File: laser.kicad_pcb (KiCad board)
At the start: 4 copper layers, 90.2 x 50.9 mm, 128 parts, among them IC201 ADM7172ACPZ-4.2-R7, IC202 LT1716CS5#TRPBF, IC203 ADM7154ARDZ-3.3-R7, IC204 IRF9358PBF, IC601 ATMEGA328P-AU, IC602 FT232RL-TUBE, IC701 MAX6126AASA25+, IC801 ADS122C04IPWR, J601 M20-9980345, J602 USB_Connector, Q401 RSR030N06TL, U101 281698-3, U201 LM4040EIM3X-2.5_NOPB, U301 OPA569AIDWPR, U302 OPA569AIDWPR, U401 ADA4528-2ACPZ-RL, U402 782853152_WE-CBA_08, U501 ADA4528-2ACPZ-RL, U502 ADA4528-2ACPZ-RL, U801 MAX5217GUA+, U802 MAX5217GUA+, Y601 ECS-160-16-33B-CKM-TR

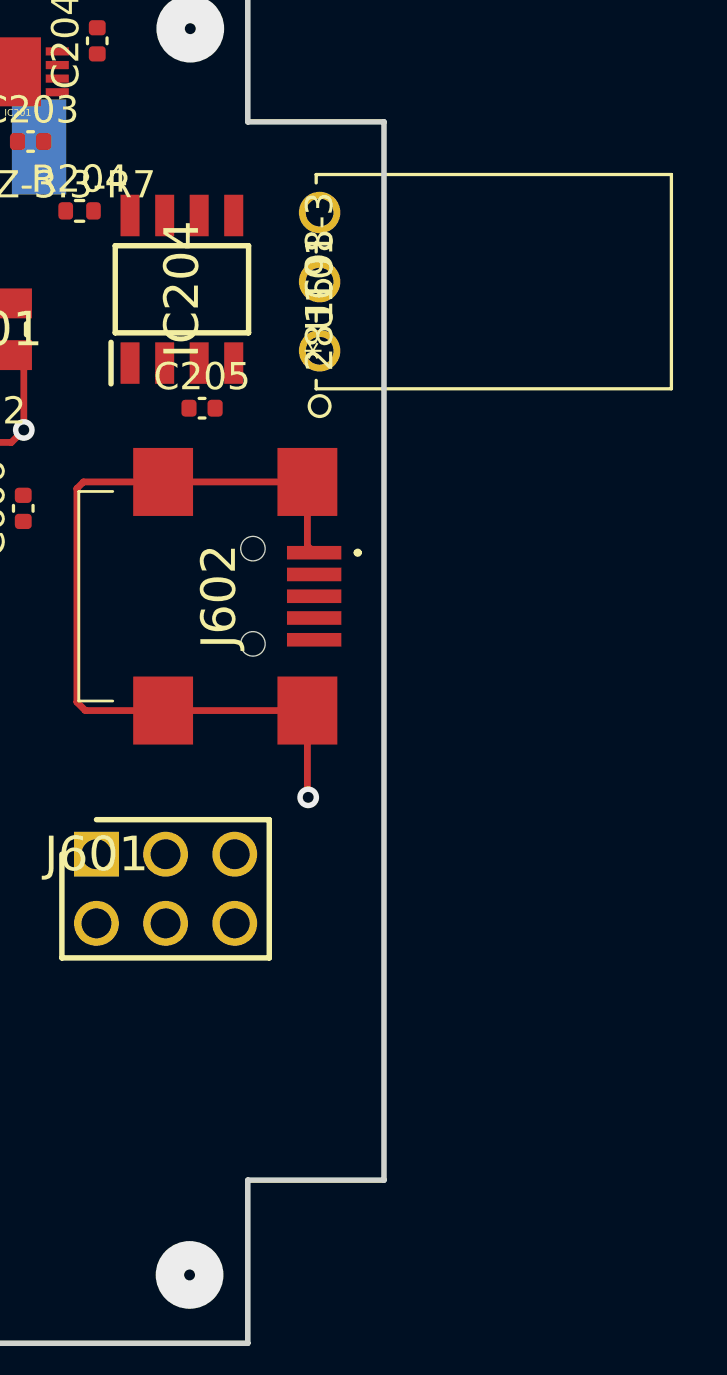
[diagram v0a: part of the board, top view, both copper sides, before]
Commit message: added 5V
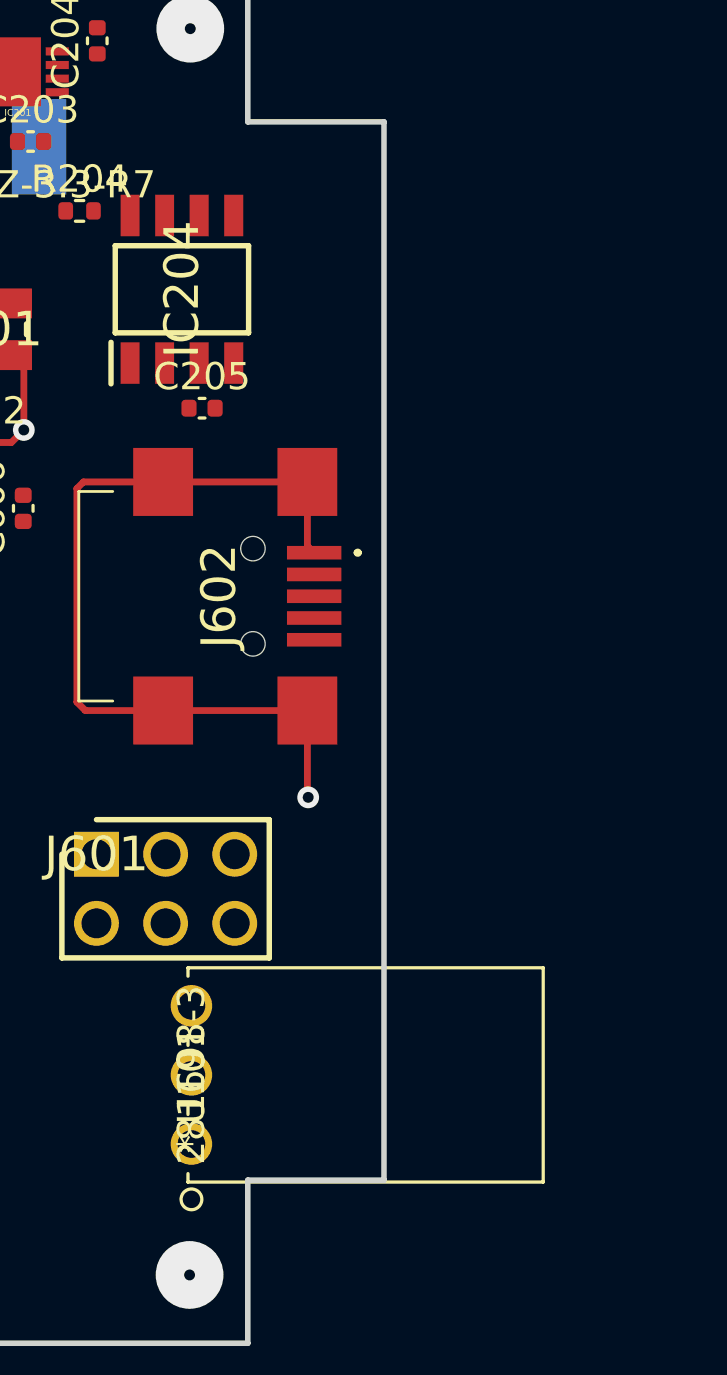
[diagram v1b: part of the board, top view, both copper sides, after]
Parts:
- moved U101 29.5 mm to (205.9, 124.9)
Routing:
- added copper zone on PWR, net 5.0V
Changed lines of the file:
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@@
     (0 F.Cu signal)
     (1 GND power hide)
-    (2 PWR power)
+    (2 PWR power hide)
     (31 B.Cu signal)
     (32 B.Adhes user)
@@
   )
   (module "footprint libraries:281698-3" (layer F.Cu)
-    (at 210.62 95.74 90)
+    (at 205.91 124.89 90)
     (fp_text reference U101 (at 2.54 0 90) (layer F.SilkS)
       (effects (font (size 1 1) (thickness 0.15)))
@@
       (effects (font (size 1 1) (thickness 0.15)))
     )
-    (fp_line (start -1.397 12.927) (end 6.477 12.927) (layer F.SilkS) (width 0.12))
-    (fp_line (start 6.477 12.927) (end 6.477 -0.127) (layer F.SilkS) (width 0.12))
-    (fp_line (start 6.477 -0.127) (end 6.167348 -0.127) (layer F.SilkS) (width 0.12))
-    (fp_line (start -1.397 -0.127) (end -1.397 12.927) (layer F.SilkS) (width 0.12))
-    (fp_line (start -1.27 12.8) (end 6.35 12.8) (layer F.Fab) (width 0.1))
-    (fp_line (start 6.35 12.8) (end 6.35 0) (layer F.Fab) (width 0.1))
-    (fp_line (start 6.35 0) (end -1.27 0) (layer F.Fab) (width 0.1))
-    (fp_line (start -1.27 0) (end -1.27 12.8) (layer F.Fab) (width 0.1))
-    (fp_line (start -1.087348 -0.127) (end -1.397 -0.127) (layer F.SilkS) (width 0.12))
-    (fp_line (start 1.452652 -0.127) (end 1.087348 -0.127) (layer F.SilkS) (width 0.12))
-    (fp_line (start 3.992652 -0.127) (end 3.627348 -0.127) (layer F.SilkS) (width 0.12))
-    (fp_line (start -1.524 -1.016) (end -1.524 13.054) (layer F.CrtYd) (width 0.05))
-    (fp_line (start -1.524 13.054) (end 6.604 13.054) (layer F.CrtYd) (width 0.05))
-    (fp_line (start 6.604 13.054) (end 6.604 -1.016) (layer F.CrtYd) (width 0.05))
-    (fp_line (start 6.604 -1.016) (end -1.524 -1.016) (layer F.CrtYd) (width 0.05))
-    (fp_circle (center -2.032 0) (end -1.651 0) (layer F.SilkS) (width 0.12))
-    (fp_circle (center -2.032 0) (end -1.651 0) (layer B.SilkS) (width 0.12))
-    (fp_circle (center 0 -1.905) (end 0.381 -1.905) (layer F.Fab) (width 0.1))
-    (fp_text user "Copyright 2021 Accelerated Designs. All rights reserved." (at 0 0 90) (layer Cmts.User)
-      (effects (font (size 0.127 0.127) (thickness 0.002)))
+    (fp_text user * (at 0 0 90) (layer F.Fab)
+      (effects (font (size 1 1) (thickness 0.15)))
     )
     (fp_text user * (at 0 0 90) (layer F.SilkS)
       (effects (font (size 1 1) (thickness 0.15)))
     )
-    (fp_text user * (at 0 0 90) (layer F.Fab)
-      (effects (font (size 1 1) (thickness 0.15)))
+    (fp_text user "Copyright 2021 Accelerated Designs. All rights reserved." (at 0 0 90) (layer Cmts.User)
+      (effects (font (size 0.127 0.127) (thickness 0.002)))
     )
-    (pad 1 thru_hole circle (at 0 0 90) (size 1.524 1.524) (drill 1.016) (layers *.Cu *.Mask)
-      (net 119 GND))
-    (pad 2 thru_hole circle (at 2.54 0 90) (size 1.524 1.524) (drill 1.016) (layers *.Cu *.Mask)
-      (net 40 5V_EXTERNAL_Power_Source))
+    (fp_circle (center 0 -1.905) (end 0.381 -1.905) (layer F.Fab) (width 0.1))
+    (fp_circle (center -2.032 0) (end -1.651 0) (layer B.SilkS) (width 0.12))
+    (fp_circle (center -2.032 0) (end -1.651 0) (layer F.SilkS) (width 0.12))
+    (fp_line (start 6.604 -1.016) (end -1.524 -1.016) (layer F.CrtYd) (width 0.05))
+    (fp_line (start 6.604 13.054) (end 6.604 -1.016) (layer F.CrtYd) (width 0.05))
+    (fp_line (start -1.524 13.054) (end 6.604 13.054) (layer F.CrtYd) (width 0.05))
+    (fp_line (start -1.524 -1.016) (end -1.524 13.054) (layer F.CrtYd) (width 0.05))
+    (fp_line (start 3.992652 -0.127) (end 3.627348 -0.127) (layer F.SilkS) (width 0.12))
+    (fp_line (start 1.452652 -0.127) (end 1.087348 -0.127) (layer F.SilkS) (width 0.12))
+    (fp_line (start -1.087348 -0.127) (end -1.397 -0.127) (layer F.SilkS) (width 0.12))
+    (fp_line (start -1.27 0) (end -1.27 12.8) (layer F.Fab) (width 0.1))
+    (fp_line (start 6.35 0) (end -1.27 0) (layer F.Fab) (width 0.1))
+    (fp_line (start 6.35 12.8) (end 6.35 0) (layer F.Fab) (width 0.1))
+    (fp_line (start -1.27 12.8) (end 6.35 12.8) (layer F.Fab) (width 0.1))
+    (fp_line (start -1.397 -0.127) (end -1.397 12.927) (layer F.SilkS) (width 0.12))
+    (fp_line (start 6.477 -0.127) (end 6.167348 -0.127) (layer F.SilkS) (width 0.12))
+    (fp_line (start 6.477 12.927) (end 6.477 -0.127) (layer F.SilkS) (width 0.12))
+    (fp_line (start -1.397 12.927) (end 6.477 12.927) (layer F.SilkS) (width 0.12))
     (pad 3 thru_hole circle (at 5.08 0 90) (size 1.524 1.524) (drill 1.016) (layers *.Cu *.Mask)
       (net 21 MODULATION_SIGNAL))
+    (pad 2 thru_hole circle (at 2.54 0 90) (size 1.524 1.524) (drill 1.016) (layers *.Cu *.Mask)
+      (net 40 5V_EXTERNAL_Power_Source))
+    (pad 1 thru_hole circle (at 0 0 90) (size 1.524 1.524) (drill 1.016) (layers *.Cu *.Mask)
+      (net 119 GND))
   )
   (module "footprint libraries:LM4040EIM3X-2.5&slash_NOPB" (layer F.Cu)
@@
       )
     )
+  )
+  (zone (net 16) (net_name 5.0V) (layer PWR) (hatch edge 0.508)
+    (connect_pads (clearance 0.508))
+    (min_thickness 0.254)
+    (fill yes (arc_segments 32) (thermal_gap 0.508) (thermal_bridge_width 0.508))
+    (polygon
+      (pts
+        (xy 208.01 132.65) (xy 201.04 132.65) (xy 201.04 119.66) (xy 187.17 119.66) (xy 187.17 81.02)
+        (xy 208.01 80.95)
+      )
+    )

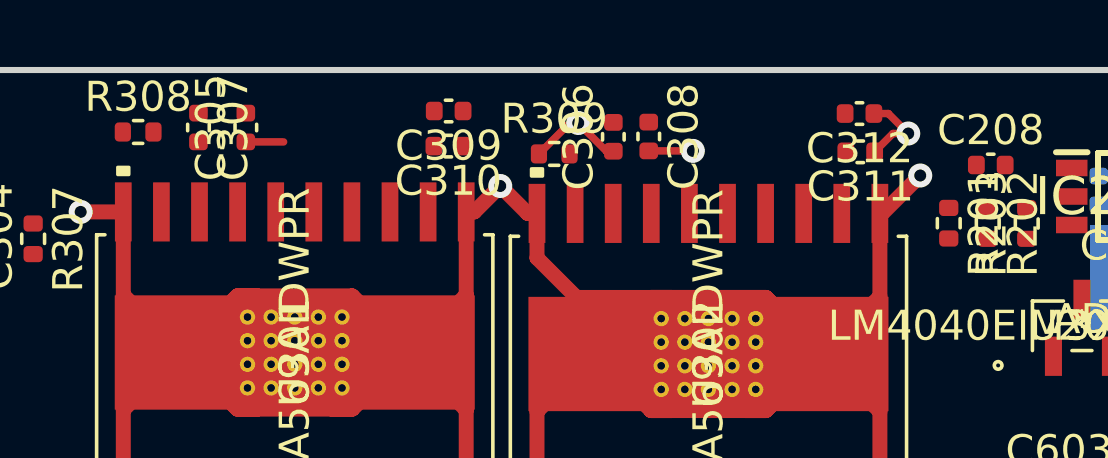
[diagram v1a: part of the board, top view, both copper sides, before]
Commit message: update power op amps sch
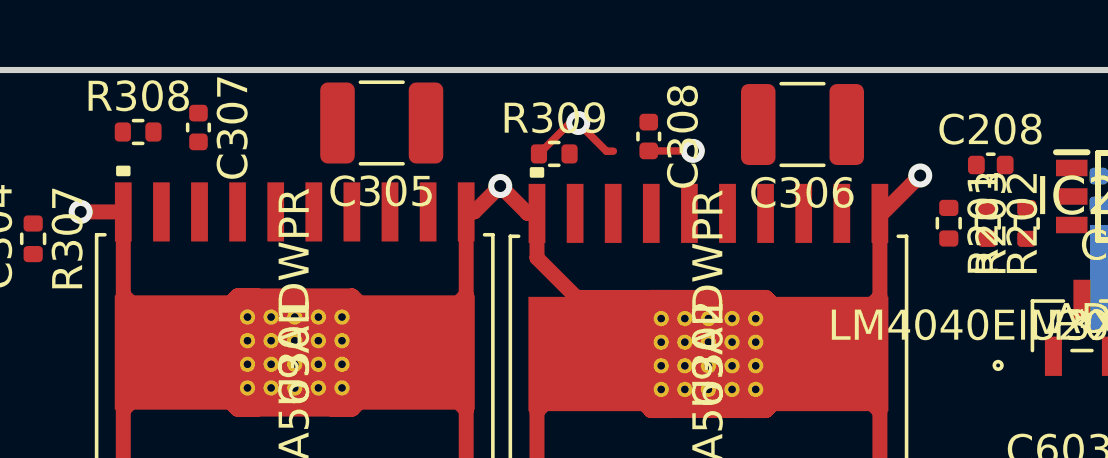
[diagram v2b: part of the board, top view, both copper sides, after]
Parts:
- removed C309, C311: 1u, Capacitor_SMD:C_0402_1005Metric
- removed C310, C312: 0.1u, Capacitor_SMD:C_0402_1005Metric
- C305, C306: footprint Capacitor_SMD:C_0402_1005Metric -> Capacitor_SMD:C_1210_3225Metric
- moved C306 6.32 mm to (180.7, 83.2), turned to 180 degrees
- moved C305 4.53 mm to (166.7, 83.1), turned to 180 degrees
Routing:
- net GND: track 208.4 -> 204.3 mm, vias 38 -> 37

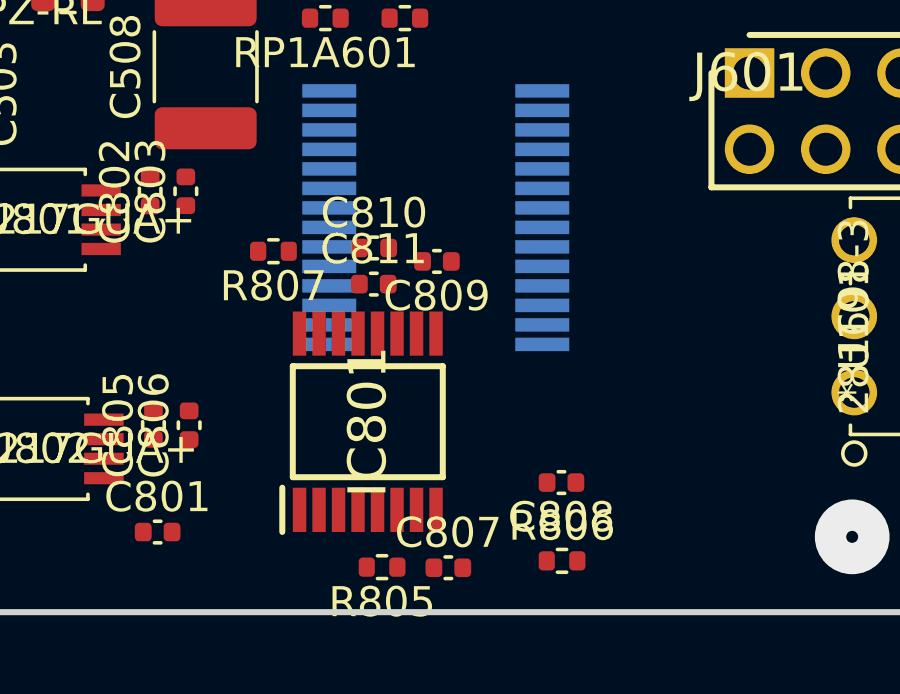
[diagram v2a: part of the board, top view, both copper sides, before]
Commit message: added 3.3
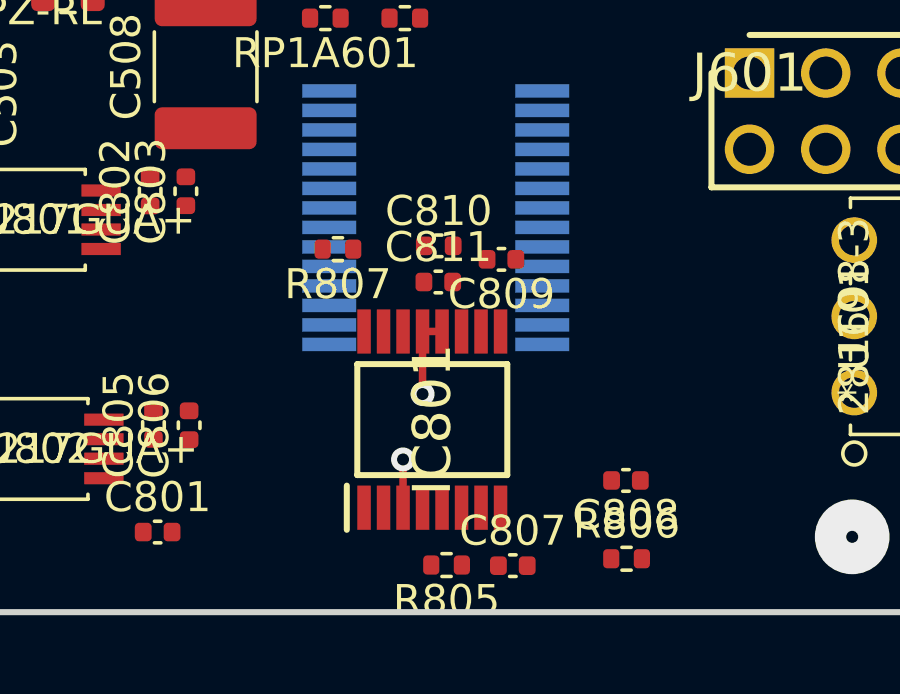
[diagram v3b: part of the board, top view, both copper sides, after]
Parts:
- moved R805 2.15 mm to (192.3, 130.6)
- moved C808 2.15 mm to (198.3, 127.8)
- moved C811 2.15 mm to (192.0, 121.2)
- moved C807 2.15 mm to (194.5, 130.7)
- moved C809 2.15 mm to (194.2, 120.5)
- moved C810 2.15 mm to (192.1, 120.0)
- moved IC801 2.15 mm to (191.8, 125.8)
- moved R806 2.15 mm to (198.3, 130.4)
- moved R807 2.15 mm to (188.7, 120.1)
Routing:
- net 3.3V: track 0.00 -> 4.35 mm, vias 0 -> 2
- added copper zone on PWR, net 3.3V

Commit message: added half a trace for 5v ext
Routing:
- net 5V_EXTERNAL_Power_Source: track 0.00 -> 31.5 mm
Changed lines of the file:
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@@
     (thickness 1.6)
     (drawings 17)
-    (tracks 191)
+    (tracks 194)
     (zones 0)
     (modules 124)
@@
   )
   (setup
-    (last_trace_width 2)
+    (last_trace_width 1.8)
     (user_trace_width 0.5)
-    (user_trace_width 2)
+    (user_trace_width 1.8)
     (trace_clearance 0.2)
     (zone_clearance 0.508)
@@
   (segment (start 190.87 127.12) (end 190.87 127.12) (width 0.25) (layer F.Cu) (net 7))
   (via (at 190.87 127.12) (size 0.8) (drill 0.4) (layers F.Cu B.Cu) (net 7))
+  (segment (start 211.700001 117.637629) (end 211.700001 93.830001) (width 1.8) (layer PWR) (net 40))
+  (segment (start 206.98763 122.35) (end 211.700001 117.637629) (width 1.8) (layer PWR) (net 40))
+  (segment (start 205.91 122.35) (end 206.98763 122.35) (width 1.8) (layer PWR) (net 40))
   (via (at 126.2634 93.2256) (size 2.4892) (drill 0.4) (layers F.Cu B.Cu) (net 119))
   (via (at 130.8354 83.9292) (size 2.4892) (drill 0.4) (layers F.Cu B.Cu) (net 119))
